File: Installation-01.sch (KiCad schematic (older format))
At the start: 2 parts, among them J1 USB_C_Receptacle_USB2.0, U1 STM32F072RBTx

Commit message: Power and USB connectivity
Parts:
- removed U1: STM32F072RBTx, Package_QFP:LQFP-64_10x10mm_P0.5mm, symbol MCU_ST_STM32F0:STM32F072RBTx
- added C1, C2, C3, C5: 100n, symbol Device:C
- added C10, C9: 100n, symbol Device:C_Small
- added C11: 4.7n, symbol Device:C_Small
- added C4, C6: 4.7u, symbol Device:C
- added C7: 10n, symbol Device:C
- added C8: 1u, symbol Device:C
- added D1: B260, Diode_SMD:D_SMB, symbol Diode:B260
- added D2: 1N914, Diode_THT:D_DO-35_SOD27_P7.62mm_Horizontal, symbol Diode:1N914
- added F1: Polyfuse_Small, symbol Device:Polyfuse_Small
- added R1, R2, R3: 22k, symbol Device:R_Small
- added U1: STM32F072CBTx, Package_QFP:LQFP-48_7x7mm_P0.5mm, symbol MCU_ST_STM32F0:STM32F072CBTx
- added U2: MCP1700-3302E_SOT23, Package_TO_SOT_SMD:SOT-23, symbol Regulator_Linear:MCP1700-3302E_SOT23
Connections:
- net labels added: 3.3V, D+, D-, GND, VBUS, VDD, VDDA, VDDIO2
- wire segments 0 -> 81
- no-connect marks 0 -> 2

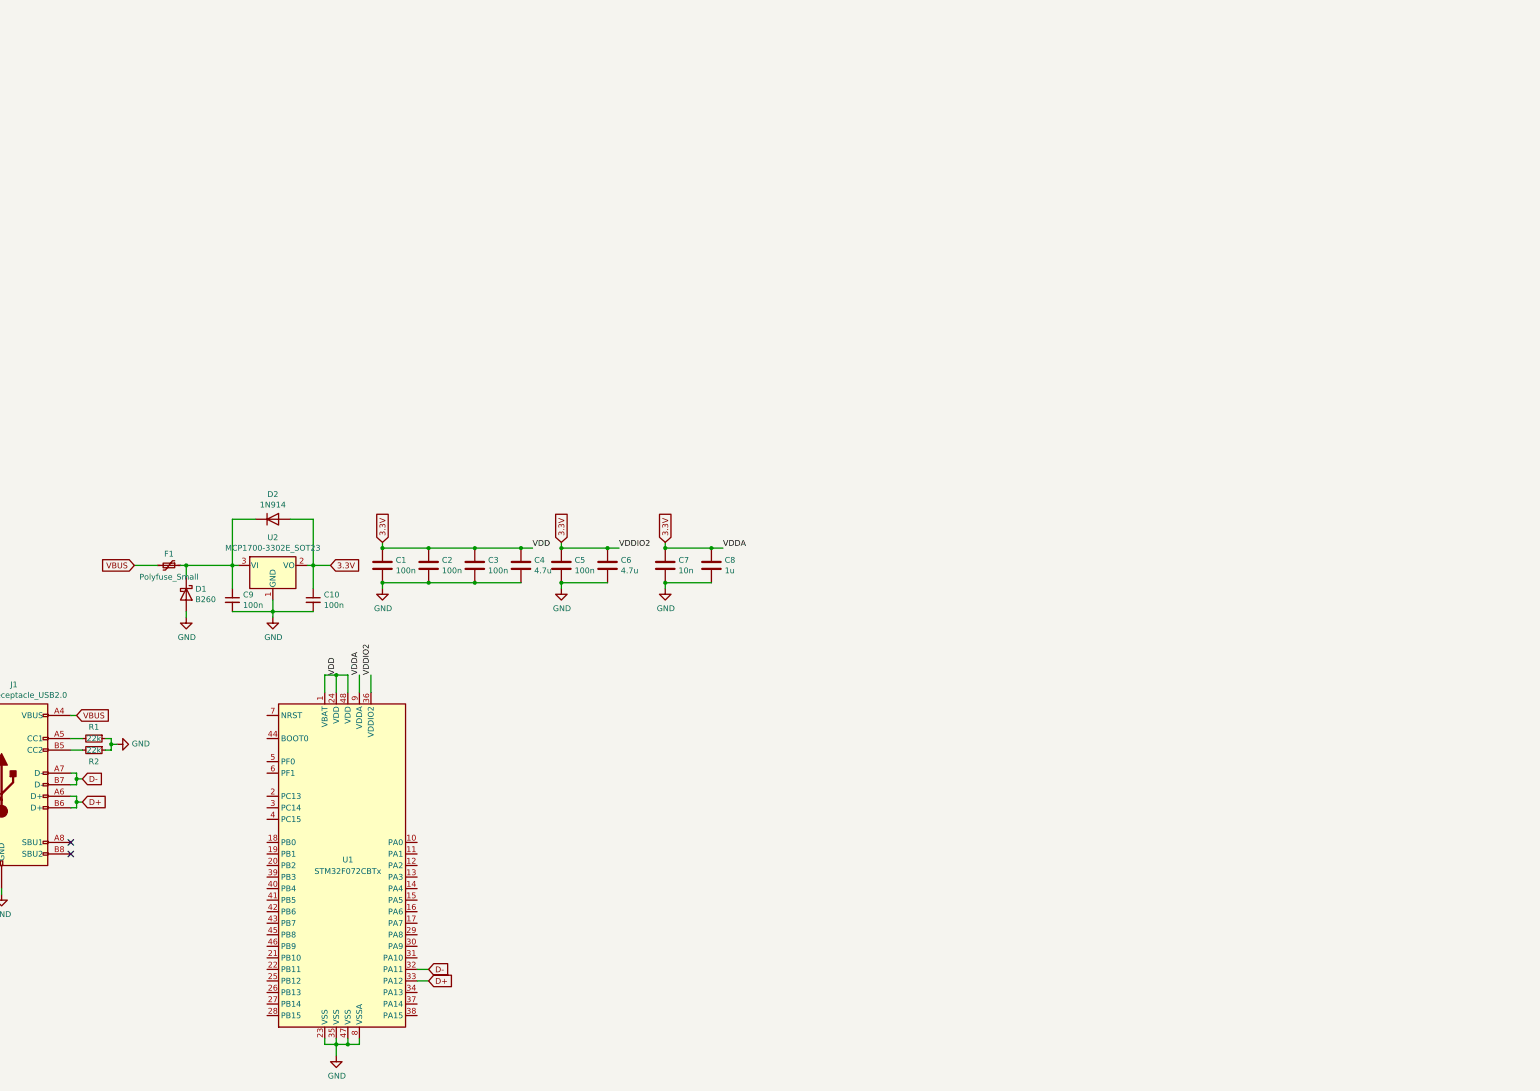
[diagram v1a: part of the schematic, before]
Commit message: matrix and led library added
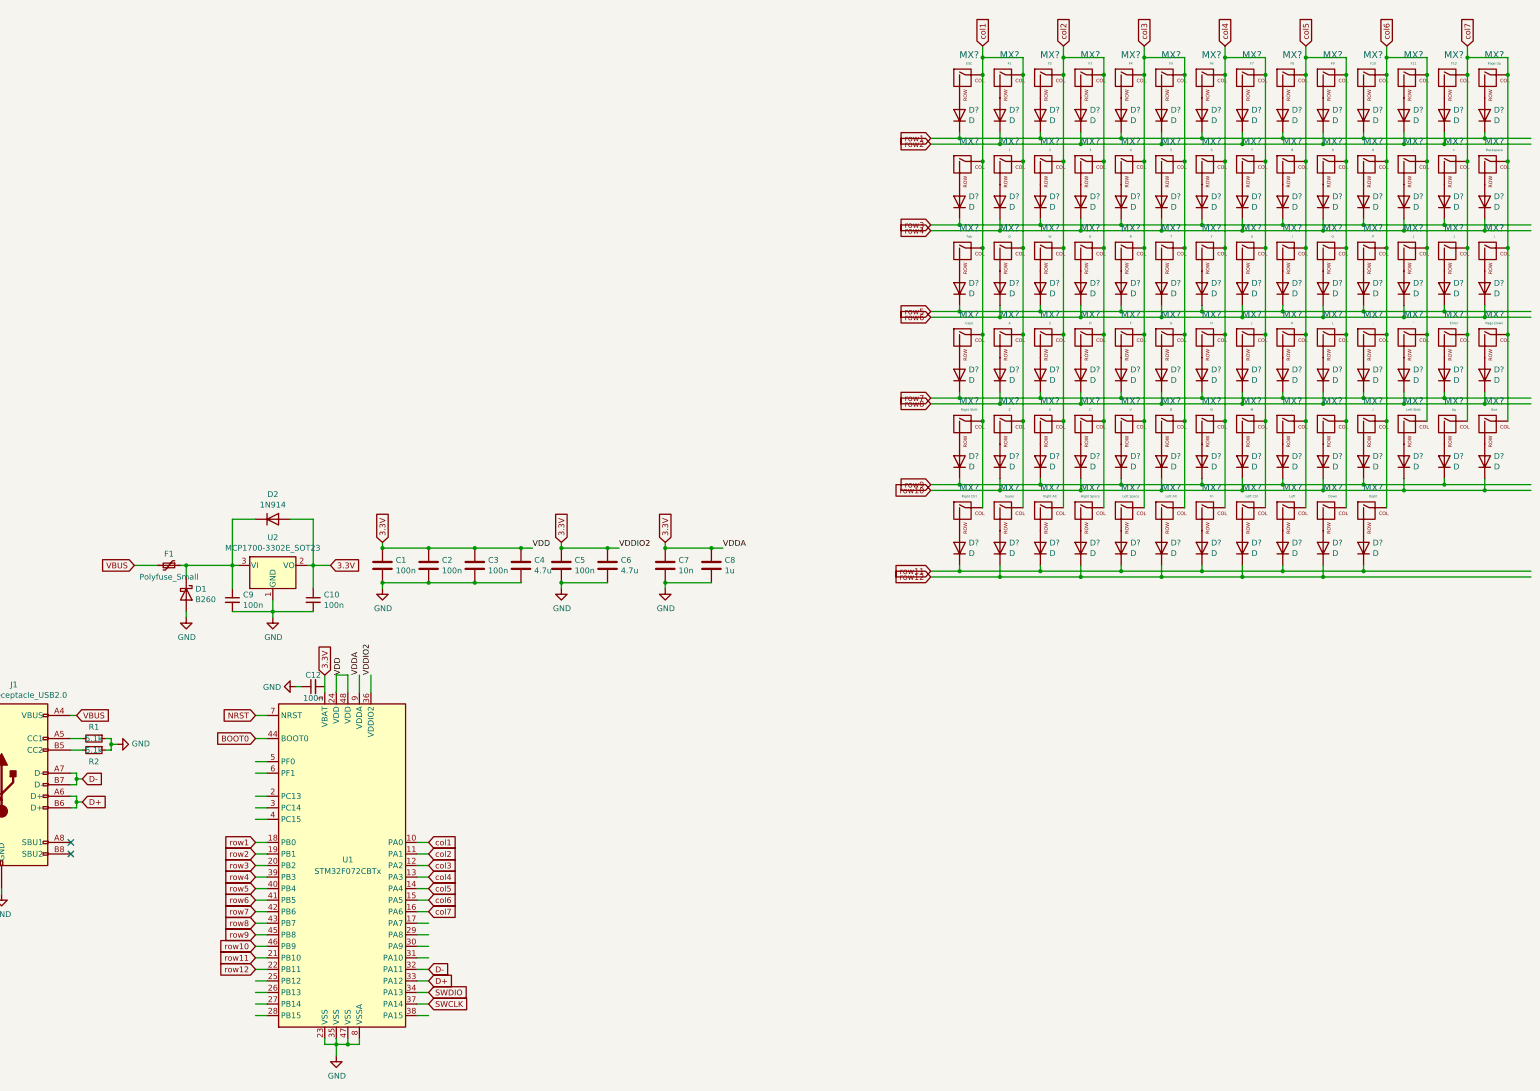
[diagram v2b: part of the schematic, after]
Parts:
- added C12: 100n, symbol Device:C_Small
- added D? (x81): D, symbol Device:D
- added MX?: ESC, symbol MX_Alps_Hybrid:MX-NoLED
- added MX?: F1, symbol MX_Alps_Hybrid:MX-NoLED
- added MX?: F2, symbol MX_Alps_Hybrid:MX-NoLED
- added MX?: F3, symbol MX_Alps_Hybrid:MX-NoLED
- added MX?: F4, symbol MX_Alps_Hybrid:MX-NoLED
- added MX?: F5, symbol MX_Alps_Hybrid:MX-NoLED
- added MX?: F6, symbol MX_Alps_Hybrid:MX-NoLED
- added MX?: F7, symbol MX_Alps_Hybrid:MX-NoLED
- added MX?: F8, symbol MX_Alps_Hybrid:MX-NoLED
- added MX?: F9, symbol MX_Alps_Hybrid:MX-NoLED
- added MX?: F10, symbol MX_Alps_Hybrid:MX-NoLED
- added MX?: F11, symbol MX_Alps_Hybrid:MX-NoLED
- added MX?: F12, symbol MX_Alps_Hybrid:MX-NoLED
- added MX?: `, symbol MX_Alps_Hybrid:MX-NoLED
- added MX?: 1, symbol MX_Alps_Hybrid:MX-NoLED
- added MX?: 2, symbol MX_Alps_Hybrid:MX-NoLED
- added MX?: 3, symbol MX_Alps_Hybrid:MX-NoLED
- added MX?: 4, symbol MX_Alps_Hybrid:MX-NoLED
- added MX?: 5, symbol MX_Alps_Hybrid:MX-NoLED
- added MX?: 6, symbol MX_Alps_Hybrid:MX-NoLED
- added MX?: 7, symbol MX_Alps_Hybrid:MX-NoLED
- added MX?: 8, symbol MX_Alps_Hybrid:MX-NoLED
- added MX?: 9, symbol MX_Alps_Hybrid:MX-NoLED
- added MX?: 0, symbol MX_Alps_Hybrid:MX-NoLED
- added MX?: -, symbol MX_Alps_Hybrid:MX-NoLED
- added MX?: =, symbol MX_Alps_Hybrid:MX-NoLED
- added MX?: Tab, symbol MX_Alps_Hybrid:MX-NoLED
- added MX?: Q, symbol MX_Alps_Hybrid:MX-NoLED
- added MX?: W, symbol MX_Alps_Hybrid:MX-NoLED
- added MX?: E, symbol MX_Alps_Hybrid:MX-NoLED
- added MX?: R, symbol MX_Alps_Hybrid:MX-NoLED
- added MX?: T, symbol MX_Alps_Hybrid:MX-NoLED
- added MX?: Y, symbol MX_Alps_Hybrid:MX-NoLED
- added MX?: U, symbol MX_Alps_Hybrid:MX-NoLED
- added MX?: I, symbol MX_Alps_Hybrid:MX-NoLED
- added MX?: O, symbol MX_Alps_Hybrid:MX-NoLED
- added MX?: P, symbol MX_Alps_Hybrid:MX-NoLED
- added MX?: [, symbol MX_Alps_Hybrid:MX-NoLED
- added MX?: ], symbol MX_Alps_Hybrid:MX-NoLED
- added MX?: Caps, symbol MX_Alps_Hybrid:MX-NoLED
- added MX?: A, symbol MX_Alps_Hybrid:MX-NoLED
- added MX?: S, symbol MX_Alps_Hybrid:MX-NoLED
- added MX?: D, symbol MX_Alps_Hybrid:MX-NoLED
- added MX?: F, symbol MX_Alps_Hybrid:MX-NoLED
- added MX?: G, symbol MX_Alps_Hybrid:MX-NoLED
- added MX?: H, symbol MX_Alps_Hybrid:MX-NoLED
- added MX?: J, symbol MX_Alps_Hybrid:MX-NoLED
- added MX?: K, symbol MX_Alps_Hybrid:MX-NoLED
- added MX?: L, symbol MX_Alps_Hybrid:MX-NoLED
- added MX?: ;, symbol MX_Alps_Hybrid:MX-NoLED
- added MX?: ', symbol MX_Alps_Hybrid:MX-NoLED
- added MX?: Enter, symbol MX_Alps_Hybrid:MX-NoLED
- added MX?: Right Shift, symbol MX_Alps_Hybrid:MX-NoLED
- added MX?: Z, symbol MX_Alps_Hybrid:MX-NoLED
- added MX?: X, symbol MX_Alps_Hybrid:MX-NoLED
- added MX?: C, symbol MX_Alps_Hybrid:MX-NoLED
- added MX?: V, symbol MX_Alps_Hybrid:MX-NoLED
- added MX?: B, symbol MX_Alps_Hybrid:MX-NoLED
- added MX?: N, symbol MX_Alps_Hybrid:MX-NoLED
- added MX?: M, symbol MX_Alps_Hybrid:MX-NoLED
- added MX?: ,, symbol MX_Alps_Hybrid:MX-NoLED
- added MX?: ., symbol MX_Alps_Hybrid:MX-NoLED
- added MX?: /, symbol MX_Alps_Hybrid:MX-NoLED
- added MX?: Left Shift, symbol MX_Alps_Hybrid:MX-NoLED
- added MX?: Up, symbol MX_Alps_Hybrid:MX-NoLED
- added MX?: Right Ctrl, symbol MX_Alps_Hybrid:MX-NoLED
- added MX?: Super, symbol MX_Alps_Hybrid:MX-NoLED
- added MX?: Right Alt, symbol MX_Alps_Hybrid:MX-NoLED
- added MX?: Right Space, symbol MX_Alps_Hybrid:MX-NoLED
- added MX?: Left Space, symbol MX_Alps_Hybrid:MX-NoLED
- added MX?: Left Alt, symbol MX_Alps_Hybrid:MX-NoLED
- added MX?: Fn, symbol MX_Alps_Hybrid:MX-NoLED
- added MX?: Left Ctrl, symbol MX_Alps_Hybrid:MX-NoLED
- added MX?: Left, symbol MX_Alps_Hybrid:MX-NoLED
- added MX?: Down, symbol MX_Alps_Hybrid:MX-NoLED
- added MX?: Right, symbol MX_Alps_Hybrid:MX-NoLED
- added MX?: Backspace, symbol MX_Alps_Hybrid:MX-NoLED
- added MX?: \\, symbol MX_Alps_Hybrid:MX-NoLED
- added MX?: Page Down, symbol MX_Alps_Hybrid:MX-NoLED
- added MX?: End, symbol MX_Alps_Hybrid:MX-NoLED
- added MX?: Page Up, symbol MX_Alps_Hybrid:MX-NoLED
- R1, R2: value 22k -> 5.1k
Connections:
- net labels added: BOOT0, NRST, SWCLK, SWDIO, col1, col2, col3, col4, col5, col6, col7, row1, row10, row11, row12, row2, row3, row4, row5, row6, row7, row8, row9
- wire segments 81 -> 387

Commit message: per key lighting added
-removed IS31FL3733 library as it existed in another library
-using SK6812MINI individually addressable RGB LED's for per key lighting
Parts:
- added C? (x96): 0.1u, symbol Device:C_Small
- added C?: 1000u, symbol Device:C_Small
- added LED? (x83): WS2812B, symbol ws2812b:WS2812B
- added R4: 500, symbol Device:R_Small
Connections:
- net labels added: 5V, 5V_1000u, 5V_RGB, RGB_LED
- wire segments 387 -> 825
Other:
- moved on the sheet: C1, C10, C11, C12, C2, C3, C4, C5, C6, C7, C8, C9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

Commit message: rgb fix and encoder library
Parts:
- added C?: 100n, symbol Device:C_Small
- added C?: 4.7n, symbol Device:C_Small
- added D3: 1N914, Diode_THT:D_DO-35_SOD27_P7.62mm_Horizontal, symbol Diode:1N914
- added E1: EC11E18244A5, symbol more-keeb-parts:EC11E18244A5-Incremental-Rotary-Encoder
- added H1: MountingHole_Pad, symbol Mechanical:MountingHole_Pad
- added H10, H2, H3, H4, H5, H6, H7, H8, H9: MountingHole, symbol Mechanical:MountingHole
- added J2: Conn_ARM_JTAG_SWD_10, symbol Connector:Conn_ARM_JTAG_SWD_10
- added R?: 1M, symbol Device:R_Small
- added U2: USBLC6-2SC6, Package_TO_SOT_SMD:SOT-23-6, symbol Power_Protection:USBLC6-2SC6
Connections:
- net labels added: CASE, Case, DBUS+, DBUS-, E_Button, E_CCW, E_CW
- wire segments 825 -> 866
- no-connect marks 2 -> 5
